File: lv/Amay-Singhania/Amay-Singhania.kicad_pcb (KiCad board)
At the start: 4 copper layers, 50 x 184 mm, 4 parts

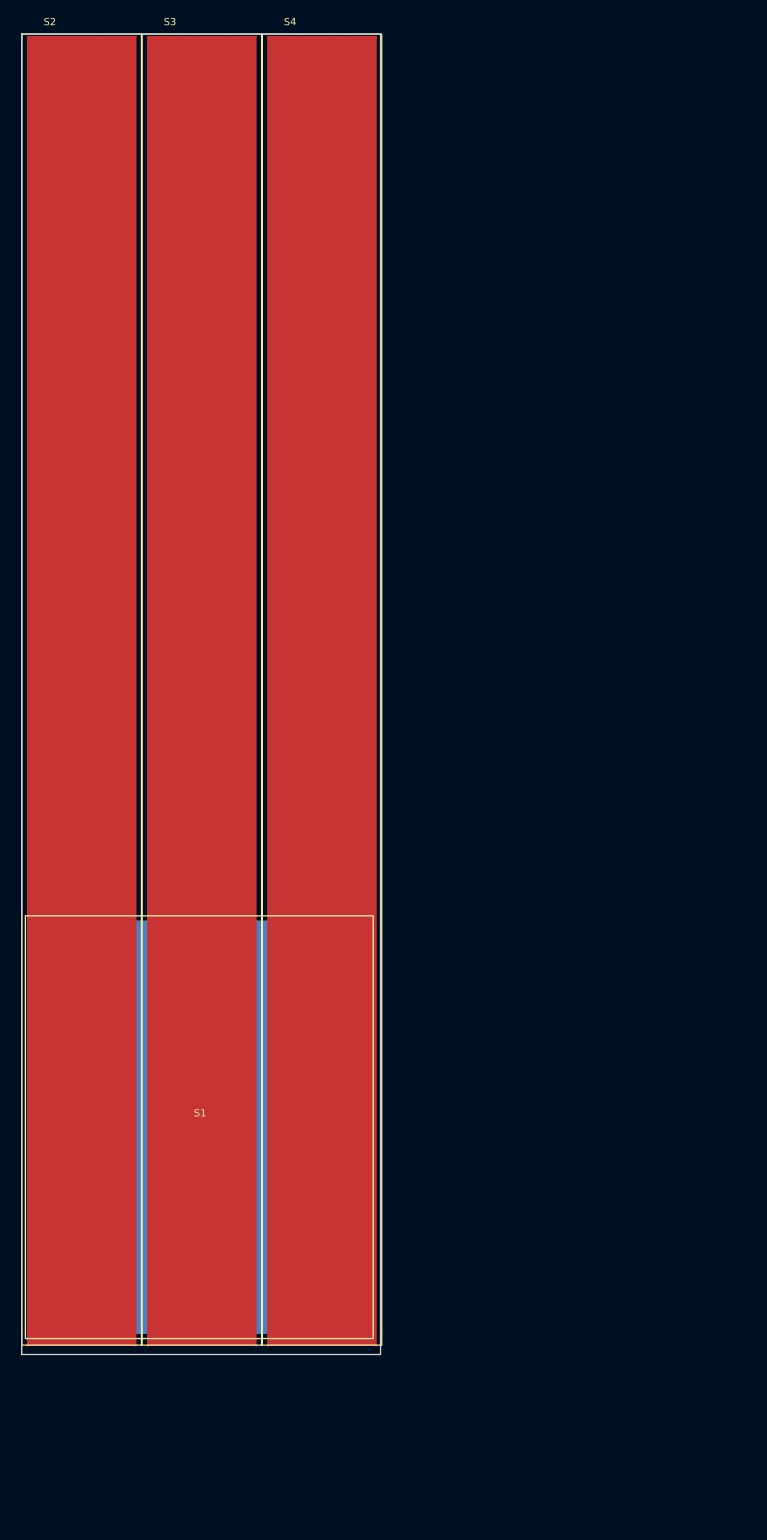
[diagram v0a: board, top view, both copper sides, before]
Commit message: Updated PCB with RC values for low pass filter. has old onboarding sheets with in-Amp and other designs, will be removed in next commit
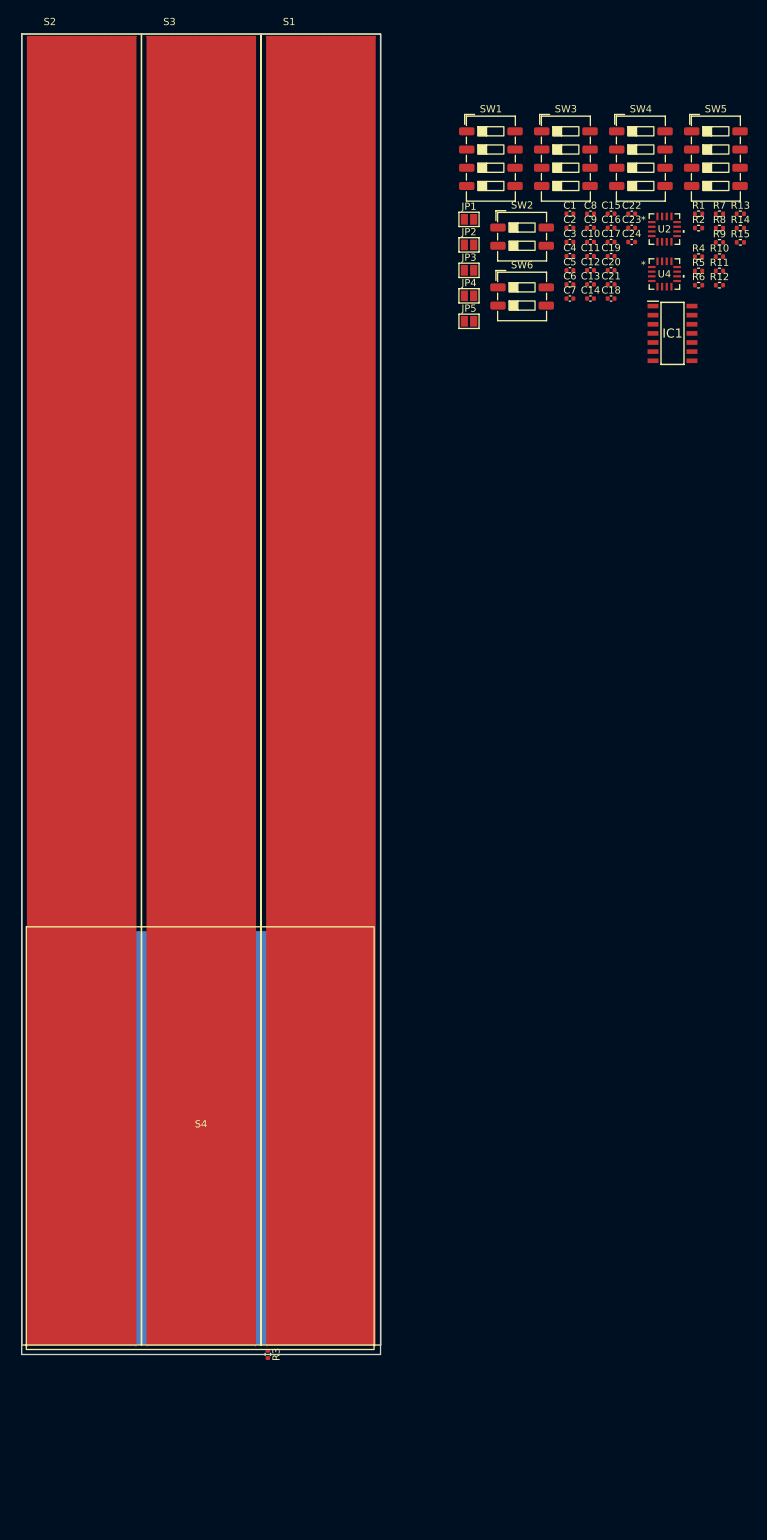
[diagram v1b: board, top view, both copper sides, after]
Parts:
- removed the S1 at (41.9, 167.9)
- added C1: 100nF, Capacitor_SMD:C_0402_1005Metric, F.Cu at (93.4, 42.0)
- added C10: 0.1uF, Capacitor_SMD:C_0402_1005Metric, F.Cu at (96.3, 46.0)
- added C11: 0.1uF, Capacitor_SMD:C_0402_1005Metric, F.Cu at (96.3, 48.0)
- added C12: 0.1uF, Capacitor_SMD:C_0402_1005Metric, F.Cu at (96.3, 49.9)
- added C13: 0.1uF, Capacitor_SMD:C_0402_1005Metric, F.Cu at (96.3, 51.9)
- added C14: 0.1uF, Capacitor_SMD:C_0402_1005Metric, F.Cu at (96.3, 53.9)
- added C15: 100nF, Capacitor_SMD:C_0402_1005Metric, F.Cu at (99.1, 42.0)
- added C16: 100nF, Capacitor_SMD:C_0402_1005Metric, F.Cu at (99.1, 44.0)
- added C17: 100nF, Capacitor_SMD:C_0402_1005Metric, F.Cu at (99.1, 46.0)
- added C18: 0.1uF, Capacitor_SMD:C_0402_1005Metric, F.Cu at (99.1, 53.9)
- added C19: C, Capacitor_SMD:C_0402_1005Metric, F.Cu at (99.1, 48.0)
- added C2: 100nF, Capacitor_SMD:C_0402_1005Metric, F.Cu at (93.4, 44.0)
- added C20: C, Capacitor_SMD:C_0402_1005Metric, F.Cu at (99.1, 49.9)
- added C21: C, Capacitor_SMD:C_0402_1005Metric, F.Cu at (99.1, 51.9)
- added C22: C, Capacitor_SMD:C_0402_1005Metric, F.Cu at (102.0, 42.0)
- added C23: C, Capacitor_SMD:C_0402_1005Metric, F.Cu at (102.0, 44.0)
- added C24: C, Capacitor_SMD:C_0402_1005Metric, F.Cu at (102.0, 46.0)
- added C3: 100nF, Capacitor_SMD:C_0402_1005Metric, F.Cu at (93.4, 46.0)
- added C4: 0.1uF, Capacitor_SMD:C_0402_1005Metric, F.Cu at (93.4, 48.0)
- added C5: 0.1uF, Capacitor_SMD:C_0402_1005Metric, F.Cu at (93.4, 49.9)
- added C6: 0.1uF, Capacitor_SMD:C_0402_1005Metric, F.Cu at (93.4, 51.9)
- added C7: 0.1uF, Capacitor_SMD:C_0402_1005Metric, F.Cu at (93.4, 53.9)
- added C8: 0.1uF, Capacitor_SMD:C_0402_1005Metric, F.Cu at (96.3, 42.0)
- added C9: 0.1uF, Capacitor_SMD:C_0402_1005Metric, F.Cu at (96.3, 44.0)
- added IC1: TLV4888DR, TLV4888DR:SOIC127P600X175-14N, F.Cu at (107.7, 58.7)
- added JP1: ~, Jumper:SolderJumper-2_P1.3mm_Open_Pad1.0x1.5mm, F.Cu at (79.3, 42.8)
- added JP2: ~, Jumper:SolderJumper-2_P1.3mm_Open_Pad1.0x1.5mm, F.Cu at (79.3, 46.4)
- added JP3: ~, Jumper:SolderJumper-2_P1.3mm_Open_Pad1.0x1.5mm, F.Cu at (79.3, 49.9)
- added JP4: ~, Jumper:SolderJumper-2_P1.3mm_Open_Pad1.0x1.5mm, F.Cu at (79.3, 53.5)
- added JP5: ~, Jumper:SolderJumper-2_P1.3mm_Open_Pad1.0x1.5mm, F.Cu at (79.3, 57.0)
- added R1: 350, Resistor_SMD:R_0402_1005Metric, F.Cu at (111.3, 42.1)
- added R10: 249R, Resistor_SMD:R_0402_1005Metric, F.Cu at (114.2, 48.0)
- added R11: R, Resistor_SMD:R_0402_1005Metric, F.Cu at (114.2, 50.0)
- added R12: R, Resistor_SMD:R_0402_1005Metric, F.Cu at (114.2, 52.0)
- added R13: R, Resistor_SMD:R_0402_1005Metric, F.Cu at (117.1, 42.1)
- added R14: R, Resistor_SMD:R_0402_1005Metric, F.Cu at (117.1, 44.0)
- added R15: R, Resistor_SMD:R_0402_1005Metric, F.Cu at (117.1, 46.0)
- added R2: 350, Resistor_SMD:R_0402_1005Metric, F.Cu at (111.3, 44.0)
- added R3: 350, Resistor_SMD:R_0402_1005Metric, F.Cu at (51.3, 201.0)
- added R4: 350, Resistor_SMD:R_0402_1005Metric, F.Cu at (111.3, 48.0)
- added R5: 350, Resistor_SMD:R_0402_1005Metric, F.Cu at (111.3, 50.0)
- added R6: 350, Resistor_SMD:R_0402_1005Metric, F.Cu at (111.3, 52.0)
- added R7: 249R, Resistor_SMD:R_0402_1005Metric, F.Cu at (114.2, 42.1)
- added R8: 249R, Resistor_SMD:R_0402_1005Metric, F.Cu at (114.2, 44.0)
- added R9: 249R, Resistor_SMD:R_0402_1005Metric, F.Cu at (114.2, 46.0)
- added S4: StrainGaugeReference, StrainGauge:ReferenceStrainGauge, F.Cu at (42.0, 169.4)
- added SW1: SW_DIP_x04, Button_Switch_SMD:SW_DIP_SPSTx04_Slide_6.7x11.72mm_W6.73mm_P2.54mm_LowProfile_JPin, F.Cu at (82.4, 34.4)
- added SW2: SW_DIP_x02, Button_Switch_SMD:SW_DIP_SPSTx02_Slide_6.7x6.64mm_W6.73mm_P2.54mm_LowProfile_JPin, F.Cu at (86.7, 45.2)
- added SW3: SW_DIP_x04, Button_Switch_SMD:SW_DIP_SPSTx04_Slide_6.7x11.72mm_W6.73mm_P2.54mm_LowProfile_JPin, F.Cu at (92.8, 34.4)
- added SW4: SW_DIP_x04, Button_Switch_SMD:SW_DIP_SPSTx04_Slide_6.7x11.72mm_W6.73mm_P2.54mm_LowProfile_JPin, F.Cu at (103.3, 34.4)
- added SW5: SW_DIP_x04, Button_Switch_SMD:SW_DIP_SPSTx04_Slide_6.7x11.72mm_W6.73mm_P2.54mm_LowProfile_JPin, F.Cu at (113.7, 34.4)
- added SW6: SW_DIP_x02, Button_Switch_SMD:SW_DIP_SPSTx02_Slide_6.7x6.64mm_W6.73mm_P2.54mm_LowProfile_JPin, F.Cu at (86.7, 53.6)
- added U2: AD8222HACPZ-R7, AD8222:CP_16_19_ADI, F.Cu at (106.6, 44.2)
- added U4: AD8222HACPZ-R7, AD8222:CP_16_19_ADI, F.Cu at (106.6, 50.4)
- moved S1 0.14 mm to (50.4, 17.0)
- moved S3 0.07 mm to (33.7, 17.0)
- renumbered S4 to S1

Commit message: wjker
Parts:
- removed C12, C13, C14, C18: 0.1uF, Capacitor_SMD:C_0402_1005Metric
- removed C15, C16, C17: 100nF, Capacitor_SMD:C_0402_1005Metric
- removed C19, C20, C21, C22, C23, C24: C, Capacitor_SMD:C_0402_1005Metric
- removed R15: R, Resistor_SMD:R_0402_1005Metric
- removed the R5 at (111.3, 50.0)
- removed SW3, SW4, SW5: SW_DIP_x04, Button_Switch_SMD:SW_DIP_SPSTx04_Slide_6.7x11.72mm_W6.73mm_P2.54mm_LowProfile_JPin
- removed SW6: SW_DIP_x02, Button_Switch_SMD:SW_DIP_SPSTx02_Slide_6.7x6.64mm_W6.73mm_P2.54mm_LowProfile_JPin
- removed U2, U4: AD8222HACPZ-R7, AD8222:CP_16_19_ADI
- added R3: 100R, Resistor_SMD:R_0402_1005Metric, F.Cu at (74.5, 192.7)
- added U1: ADS122C14IRTER, ADS122C14:RTE0016C-IPC_A, F.Cu at (91.3, 193.7)
- C1: value 100nF -> 0.1uF
- C10, C11, C9: value 0.1uF -> 100nF
- C2: value 100nF -> 10uF
- C3: value 100nF -> 100uF
- C4, C5, C6, C8: value 0.1uF -> 10uF
- R10, R9: value 249R -> 100R
- R11: value R -> 350
- R12: value R -> 100R
- R13, R14: value R -> 4.7kR
- R4: value 350 -> 10kR
- R6: value 350 -> 100R
- R7, R8: value 249R -> 350
- moved R14 153.2 mm to (80.3, 192.7)
- moved R13 153.2 mm to (80.3, 190.7)
- moved R1 151.2 mm to (74.5, 188.7)
- moved R10 151.2 mm to (77.4, 194.7)
- moved R11 151.2 mm to (77.4, 196.7)
- moved R2 151.2 mm to (74.5, 190.7)
- moved R4 151.2 mm to (74.5, 194.7)
- moved R7 151.2 mm to (77.4, 188.7)
- moved R8 151.2 mm to (77.4, 190.7)
- moved R9 151.2 mm to (77.4, 192.7)
- moved R6 149.3 mm to (74.5, 196.7)
- moved R12 140.9 mm to (80.3, 188.7)
- moved C10 140.4 mm to (92.1, 186.3)
- moved C11 140.4 mm to (92.1, 188.3)
- moved C8 140.4 mm to (92.1, 182.4)
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- renumbered R3 to R5
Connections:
- C1 pad 1: +3V3 -> +5V
- C10 pad 2: Net-(C10-Pad2) -> GND
- C11 pad 1: +3V3 -> GND
- C2 pad 1: +3V3 -> GND
- C2 pad 2: GND -> Reference_Gauge
- C3 pad 2: Net-(U1-REFOUT) (its old number) -> Reference_Gauge_Filtered
- C4 pad 1: +3V3 -> GND
- C4 pad 2: Net-(C4-Pad2) -> Center_Gauge
- C5 pad 1: +3V3 -> GND
- C5 pad 2: Net-(C5-Pad2) -> Right_Gauge
- C6 pad 2: Net-(C6-Pad2) -> Left_Gauge
- C7 pad 1: +3V3 -> Net-(IC1-V-)
- C7 pad 2: Net-(C7-Pad2) -> GND
- C8 pad 1: +3V3 -> GND
- C8 pad 2: GND -> 1V65
- IC1 pad 1: Reference Gauge Out -> Reference_Gauge_Out
- IC1 pad 10: Right Axial Gauge Unbuffered -> Right_Gauge_Unbuffered
- IC1 pad 12: Left Axial Gauge Unbuffered -> Left_Gauge_Unbuffered
- IC1 pad 13: Left Axial Gauge Out -> Left_Gauge_Out
- IC1 pad 14: Left Axial Gauge Out -> Left_Gauge_Out
- IC1 pad 2: Reference Gauge Out -> Reference_Gauge_Out
- IC1 pad 3: Reference Gauge Unbuffered -> Reference_Gauge_Unbuffered
- IC1 pad 5: Center Axial Gauge Unbuffered -> Center_Gauge_Unbuffered
- IC1 pad 6: Center Axial Gauge Out -> Center_Gauge_Out
- IC1 pad 7: Center Axial Gauge Out -> Center_Gauge_Out
- IC1 pad 8: Right Axial Gauge Out -> Right_Gauge_Out
- IC1 pad 9: Right Axial Gauge Out -> Right_Gauge_Out
- JP1 pad 1: SG Reference Filtered -> Center_Gauge
- JP1 pad 2: Net-(U1-AIN1) -> Center_Gauge_Out
- JP2 pad 1: Net-(U1-AIN1) -> Right_Gauge
- JP2 pad 2: 1V65 -> Right_Gauge_Out
- JP3 pad 1: Center Axial Gauge -> Left_Gauge
- JP3 pad 2: Center Axial Gauge Out -> Left_Gauge_Out
- JP4 pad 1: Right Axial Gauge -> Reference_Gauge_Filtered
- JP4 pad 2: Right Axial Gauge Out -> Net-(U1-AIN1)
- JP5 pad 1: Left Axial Gauge -> Net-(U1-AIN1)
- JP5 pad 2: Left Axial Gauge Out -> 1V65
- R1 pad 2: 1V65 -> 1V65_Unfiltered
- R10 pad 1: Net-(R10-Pad1) -> Left_Gauge_Out
- R10 pad 2: Net-(R10-Pad2) -> Left_Gauge
- R11 pad 1: SG Reference -> Reference_Gauge_Unbuffered
- R11 pad 2: Reference Gauge Out -> GND
- R12 pad 1: SG Reference Filtered -> 1V65
- R12 pad 2: Reference Gauge Out -> 1V65_Unfiltered
- R13 pad 1: Center Axial Gauge Out -> +3V3
- R13 pad 2: Center Axial Gauge -> ADC_SCL
- R14 pad 1: Right Axial Gauge Out -> +3V3
- R14 pad 2: Right Axial Gauge -> ADC_SDA
- R2 pad 1: 1V65 -> 1V65_Unfiltered
- R4 pad 1: Left Axial Gauge Unbuffered -> Reference_Gauge_Filtered
- R4 pad 2: GND -> Reference_Gauge_Out
- R5 pad 1: Center Axial Gauge Unbuffered -> Center_Gauge_Unbuffered
- R6 pad 1: Reference Gauge Unbuffered -> Center_Gauge_Out
- R6 pad 2: GND -> Center_Gauge
- R7 pad 1: Net-(R7-Pad1) -> Left_Gauge_Unbuffered
- R7 pad 2: Net-(R7-Pad2) -> GND
- R8 pad 1: Net-(R8-Pad1) -> Right_Gauge_Unbuffered
- R8 pad 2: Net-(R8-Pad2) -> GND
- R9 pad 1: Net-(R9-Pad1) -> Right_Gauge_Out
- R9 pad 2: Net-(R9-Pad2) -> Right_Gauge
- SW1 pad 5: GND -> +3V3
- SW1 pad 6: +3V3 -> GND
- SW1 pad 7: ADC SCL -> ADC_SCL
- SW1 pad 8: ADC SDA -> ADC_SDA
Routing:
- net (no net): track 0.00 -> 100.8 mm
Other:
- board size 50 x 184 mm -> 50 x 207.8 mm
- copper layers 4 -> 2

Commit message: added voltage regulators and finished schematic
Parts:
- moved R7 58.9 mm to (19.7, 201.0)
- moved R8 42.2 mm to (36.4, 200.9)
- moved R12 32.0 mm to (49.9, 213.2)
- renumbered C8 to C5, C5 to C6, C6 to C7, C7 to C8, R12 to R11, R11 to R12
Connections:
- S4 pad 2: (no net) -> +3V3
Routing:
- net (no net): track 100.8 -> 0.00 mm
- net +3V3: track 0.00 -> 82.6 mm, vias 0 -> 1
- net Reference_Gauge_Unbuffered: track 0.00 -> 17.2 mm, vias 0 -> 1
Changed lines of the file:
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@@
 		(descr "Capacitor SMD 0402 (1005 Metric), square (rectangular) end terminal, IPC-7351 nominal, (Body size source: IPC-SM-782 page 76, https://www.pcb-3d.com/wordpress/wp-content/uploads/ipc-sm-782a_amendment_1_and_2.pdf)")
 		(tags "capacitor")
-		(property "Reference" "C6"
+		(property "Reference" "C7"
 			(at 0 -1.16 0)
 			(layer "F.SilkS")
@@
 		(descr "Resistor SMD 0402 (1005 Metric), square (rectangular) end terminal, IPC-7351 nominal, (Body size source: IPC-SM-782 page 72, https://www.pcb-3d.com/wordpress/wp-content/uploads/ipc-sm-782a_amendment_1_and_2.pdf)")
 		(tags "resistor")
-		(property "Reference" "R12"
+		(property "Reference" "R11"
 			(at 0 -1.17 0)
 			(layer "F.SilkS")
@@
 		(descr "Capacitor SMD 0402 (1005 Metric), square (rectangular) end terminal, IPC-7351 nominal, (Body size source: IPC-SM-782 page 76, https://www.pcb-3d.com/wordpress/wp-content/uploads/ipc-sm-782a_amendment_1_and_2.pdf)")
 		(tags "capacitor")
-		(property "Reference" "C8"
+		(property "Reference" "C5"
 			(at 0 -1.16 0)
 			(layer "F.SilkS")
@@
 		(descr "Capacitor SMD 0402 (1005 Metric), square (rectangular) end terminal, IPC-7351 nominal, (Body size source: IPC-SM-782 page 76, https://www.pcb-3d.com/wordpress/wp-content/uploads/ipc-sm-782a_amendment_1_and_2.pdf)")
 		(tags "capacitor")
-		(property "Reference" "C5"
+		(property "Reference" "C6"
 			(at 0 -1.16 0)
 			(layer "F.SilkS")
@@
 		(sheetname "/Strain Gauges + Buffer/")
 		(sheetfile "Amay-Singhania.kicad_sch")
+		(units
+			(unit
+				(name "A")
+				(pins "1" "2")
+			)
+		)
 		(attr smd)
 		(duplicate_pad_numbers_are_jumpers no)
@@
 		)
 		(pad "1" smd rect
-			(at 23.03 58.85)
+			(at 25 58.909998)
 			(size 0.38 1.27)
 			(layers "B.Cu" "B.Mask" "B.Paste")
@@
 		)
 		(pad "2" smd rect
-			(at 30.47 0.16)
+			(at 48.22 0.12)
 			(size 0.38 1.27)
 			(layers "B.Cu" "B.Mask" "B.Paste")
+			(net "+3V3")
+			(pintype "passive")
 			(clearance 0.0762)
 		)
@@
 	(footprint "Resistor_SMD:R_0402_1005Metric"
 		(layer "F.Cu")
-		(at 77.365 190.725)
+		(at 36.41 200.95)
 		(descr "Resistor SMD 0402 (1005 Metric), square (rectangular) end terminal, IPC-7351 nominal, (Body size source: IPC-SM-782 page 72, https://www.pcb-3d.com/wordpress/wp-content/uploads/ipc-sm-782a_amendment_1_and_2.pdf)")
 		(tags "resistor")
@@
 	(footprint "Resistor_SMD:R_0402_1005Metric"
 		(layer "F.Cu")
-		(at 77.365 188.735)
+		(at 19.71 200.975)
 		(descr "Resistor SMD 0402 (1005 Metric), square (rectangular) end terminal, IPC-7351 nominal, (Body size source: IPC-SM-782 page 72, https://www.pcb-3d.com/wordpress/wp-content/uploads/ipc-sm-782a_amendment_1_and_2.pdf)")
 		(tags "resistor")
@@
 	(footprint "Resistor_SMD:R_0402_1005Metric"
 		(layer "F.Cu")
-		(at 77.365 196.695)
+		(at 49.875 213.15)
 		(descr "Resistor SMD 0402 (1005 Metric), square (rectangular) end terminal, IPC-7351 nominal, (Body size source: IPC-SM-782 page 72, https://www.pcb-3d.com/wordpress/wp-content/uploads/ipc-sm-782a_amendment_1_and_2.pdf)")
 		(tags "resistor")
-		(property "Reference" "R11"
+		(property "Reference" "R12"
 			(at 0 -1.17 0)
 			(layer "F.SilkS")
@@
 		(descr "Capacitor SMD 0402 (1005 Metric), square (rectangular) end terminal, IPC-7351 nominal, (Body size source: IPC-SM-782 page 76, https://www.pcb-3d.com/wordpress/wp-content/uploads/ipc-sm-782a_amendment_1_and_2.pdf)")
 		(tags "capacitor")
-		(property "Reference" "C7"
+		(property "Reference" "C8"
 			(at 0 -1.16 0)
 			(layer "F.SilkS")
@@
 		(layer "Edge.Cuts")
 	)
+	(via
+		(at 43.35 201.875)
+		(size 0.508)
+		(drill 0.254)
+		(layers "F.Cu" "B.Cu")
+		(net "+3V3")
+	)
 	(segment
-		(start 66.325 141.95)
-		(end 66.325 200.414087)
-		(width 0.254)
+		(start 65.880499 142.245)
+		(end 66.375 142.739501)
+		(width 0.508)
 		(layer "B.Cu")
-		(net "")
+		(net "+3V3")
 	)
 	(segment
-		(start 47.98 141.95)
-		(end 66.325 141.95)
-		(width 0.254)
+		(start 66.009906 200.915094)
+		(end 44.309906 200.915094)
+		(width 0.508)
 		(layer "B.Cu")
-		(net "")
+		(net "+3V3")
 	)
 	(segment
-		(start 43.475 200.9)
-		(end 43.15 201.225)
-		(width 0.254)
+		(start 44.309906 200.915094)
+		(end 43.35 201.875)
+		(width 0.508)
+		(layer "B.Cu")
+		(net "+3V3")
+	)
+	(segment
+		(start 66.375 200.55)
+		(end 66.009906 200.915094)
+		(width 0.508)
 		(layer "B.Cu")
-		(net "")
+		(net "+3V3")
+	)
+	(segment
+		(start 66.375 142.739501)
+		(end 66.375 200.55)
+		(width 0.508)
+		(layer "B.Cu")
+		(net "+3V3")
+	)
+	(segment
+		(start 65.395 142.245)
+		(end 65.880499 142.245)
+		(width 0.508)
+		(layer "B.Cu")
+		(net "+3V3")
+	)
+	(segment
+		(start 49.365 213.15)
+		(end 48.55 213.15)
+		(width 0.254)
+		(layer "F.Cu")
+		(net "Reference_Gauge_Unbuffered")
+	)
+	(segment
+		(start 48.55 213.15)
+		(end 47.675 212.275)
+		(width 0.254)
+		(layer "F.Cu")
+		(net "Reference_Gauge_Unbuffered")
+	)
+	(via
+		(at 47.675 212.275)
+		(size 0.508)
+		(drill 0.254)
+		(layers "F.Cu" "B.Cu")
+		(net "Reference_Gauge_Unbuffered")
 	)
 	(segment
-		(start 65.839087 200.9)
-		(end 43.475 200.9)
+		(start 44.9 212.275)
+		(end 42.175 209.55)
 		(width 0.254)
 		(layer "B.Cu")
-		(net "")
+		(net "Reference_Gauge_Unbuffered")
 	)
 	(segment
-		(start 66.325 200.414087)
-		(end 65.839087 200.9)
+		(start 47.675 212.275)
+		(end 44.9 212.275)
 		(width 0.254)
 		(layer "B.Cu")
-		(net "")
+		(net "Reference_Gauge_Unbuffered")
 	)
 	(segment
-		(start 47.645 142.285)
-		(end 47.98 141.95)
+		(start 42.175 209.55)
+		(end 42.175 201.034998)
 		(width 0.254)
 		(layer "B.Cu")
-		(net "")
+		(net "Reference_Gauge_Unbuffered")
 	)
 	(embedded_fonts no)

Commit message: PCB changes
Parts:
- added U1: SL7550-3, Package_TO_SOT_SMD:SOT-23-3, F.Cu at (100.6, 196.9)
- added U2: LDK320AM33R, LDK320AM33R:SOT23-5L_STM, F.Cu at (107.2, 190.0)
- C2: renamed from C4; value 10uF -> 0.1uF
- C3: renamed from C5; value 10uF -> 0.1uF
- C5: renamed from C2; value 10uF -> 0.1uF
- C6, C7: value 10uF -> 0.1uF
- R11: renamed from R9; value 100R -> 470R
- R12: renamed from R10; value 100R -> 470R
- R3: renamed from R11; value 100R -> 470R
- R4: renamed from R6; value 100R -> 470R
- R8: renamed from R3; value 100R -> 470R
- moved U3 4.23 mm to (95.0, 195.8)
- renumbered C3 to C4, R7 to R10, R8 to R13, R12 to R14, R4 to R5, R13 to R6, R5 to R7, R14 to R9, U1 to U3
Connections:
- net 1V65_Unfiltered renamed Net-(R1-Pad2)
- net Center_Gauge_Out renamed Net-(IC1--IN_B)
- net Left_Gauge_Out renamed Net-(IC1--IN_D)
- net Reference_Gauge_Out renamed Net-(IC1--IN_A)
- net Right_Gauge_Out renamed Net-(IC1--IN_C)
